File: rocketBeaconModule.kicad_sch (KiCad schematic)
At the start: 38 parts, among them J1 TYPE-C-31-M-12, U1 STM32F401CCU6, U2 CP2102N-Axx-xQFN20, Y1 16MHz

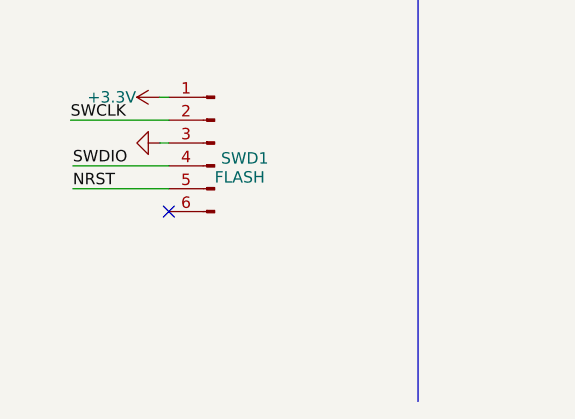
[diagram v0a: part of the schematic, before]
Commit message: added power pads
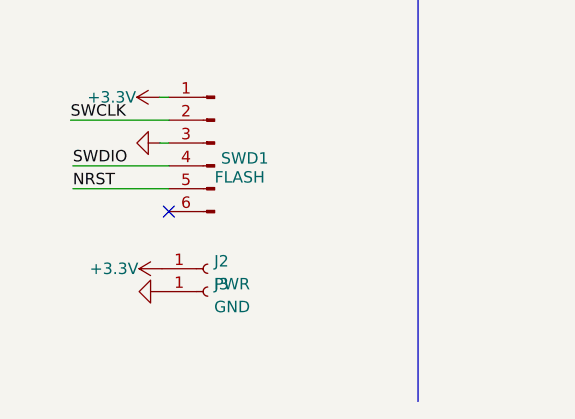
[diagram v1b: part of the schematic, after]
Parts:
- added J2: PWR, TestPoint:TestPoint_THTPad_4.0x4.0mm_Drill2.0mm, symbol Connector:Conn_01x01_Female
- added J3: GND, TestPoint:TestPoint_THTPad_4.0x4.0mm_Drill2.0mm, symbol Connector:Conn_01x01_Female
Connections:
- net +3.3V: now also J2.1 (Pin_1)
- net GND: now also J3.1 (Pin_1)
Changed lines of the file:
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@@
+    (pin "1")
+  )
+  (symbol (lib_id "power:+3.3V") (at 27.432 183.388 90) (unit 1)
+    (in_bom yes) (on_board yes)
+    (property "Reference" "#PWR0116" (id 0) (at 31.242 183.388 0)
+      (effects (font (size 1.27 1.27)) hide)
+    )
+    (property "Value" "+3.3V" (id 1) (at 22.098 183.388 90))
+    (property "Footprint" "" (id 2) (at 27.432 183.388 0)
+      (effects (font (size 1.27 1.27)) hide)
+    )
+    (property "Datasheet" "" (id 3) (at 27.432 183.388 0)
+      (effects (font (size 1.27 1.27)) hide)
+    )
     (pin "1")
   )
@@
     )
     (property "Datasheet" "" (id 3) (at 231.648 80.518 0)
+      (effects (font (size 1.27 1.27)) hide)
+    )
+    (pin "1")
+  )
+  (symbol (lib_id "Connector:Conn_01x01_Female") (at 32.512 183.388 0) (unit 1)
+    (in_bom yes) (on_board yes) (fields_autoplaced)
+    (property "Reference" "J2" (id 0) (at 33.2232 182.5533 0)
+      (effects (font (size 1.27 1.27)) (justify left))
+    )
+    (property "Value" "PWR" (id 1) (at 33.2232 185.0902 0)
+      (effects (font (size 1.27 1.27)) (justify left))
+    )
+    (property "Footprint" "TestPoint:TestPoint_THTPad_4.0x4.0mm_Drill2.0mm" (id 2) (at 32.512 183.388 0)
+      (effects (font (size 1.27 1.27)) hide)
+    )
+    (property "Datasheet" "~" (id 3) (at 32.512 183.388 0)
       (effects (font (size 1.27 1.27)) hide)
     )
@@
     (pin "2")
   )
+  (symbol (lib_id "power:GND") (at 27.432 185.928 270) (unit 1)
+    (in_bom yes) (on_board yes) (fields_autoplaced)
+    (property "Reference" "#PWR0117" (id 0) (at 21.082 185.928 0)
+      (effects (font (size 1.27 1.27)) hide)
+    )
+    (property "Value" "GND" (id 1) (at 22.352 185.928 0)
+      (effects (font (size 1.27 1.27)) hide)
+    )
+    (property "Footprint" "" (id 2) (at 27.432 185.928 0)
+      (effects (font (size 1.27 1.27)) hide)
+    )
+    (property "Datasheet" "" (id 3) (at 27.432 185.928 0)
+      (effects (font (size 1.27 1.27)) hide)
+    )
+    (pin "1")
+  )
   (symbol (lib_id "power:+3.3V") (at 237.236 145.542 90) (unit 1)
     (in_bom yes) (on_board yes)
@@
     )
     (property "Datasheet" "" (id 3) (at 237.236 145.542 0)
+      (effects (font (size 1.27 1.27)) hide)
+    )
+    (pin "1")
+  )
+  (symbol (lib_id "Connector:Conn_01x01_Female") (at 32.512 185.928 0) (unit 1)
+    (in_bom yes) (on_board yes) (fields_autoplaced)
+    (property "Reference" "J3" (id 0) (at 33.2232 185.0933 0)
+      (effects (font (size 1.27 1.27)) (justify left))
+    )
+    (property "Value" "GND" (id 1) (at 33.2232 187.6302 0)
+      (effects (font (size 1.27 1.27)) (justify left))
+    )
+    (property "Footprint" "TestPoint:TestPoint_THTPad_4.0x4.0mm_Drill2.0mm" (id 2) (at 32.512 185.928 0)
+      (effects (font (size 1.27 1.27)) hide)
+    )
+    (property "Datasheet" "~" (id 3) (at 32.512 185.928 0)
       (effects (font (size 1.27 1.27)) hide)
     )
@@
       (reference "#PWR0115") (unit 1) (value "+3.3V") (footprint "")
     )
+    (path "/50559c8e-8b0e-41f0-99d6-b5a806ac8722"
+      (reference "#PWR0116") (unit 1) (value "+3.3V") (footprint "")
+    )
+    (path "/79e3543b-cf5c-49ac-8461-e5ea63f0cfbf"
+      (reference "#PWR0117") (unit 1) (value "GND") (footprint "")
+    )
     (path "/0ce93c00-e125-4297-8f4f-84288d9bed20"
       (reference "C1") (unit 1) (value "4.7uF") (footprint "Capacitor_SMD:C_0603_1608Metric")
@@
       (reference "J1") (unit 1) (value "TYPE-C-31-M-12") (footprint "usbc:HRO_TYPE-C-31-M-12")
     )
+    (path "/64d1ad8a-ccb6-4332-9fde-cca7c83035f2"
+      (reference "J2") (unit 1) (value "PWR") (footprint "TestPoint:TestPoint_THTPad_4.0x4.0mm_Drill2.0mm")
+    )
+    (path "/7d013029-79b1-46c3-8038-ebb027ea4167"
+      (reference "J3") (unit 1) (value "GND") (footprint "TestPoint:TestPoint_THTPad_4.0x4.0mm_Drill2.0mm")
+    )
     (path "/dfcafdf4-f213-4518-865d-ab9ee2b88e54/a901ecb2-8365-4aa2-b92a-22f9aa9420f4"

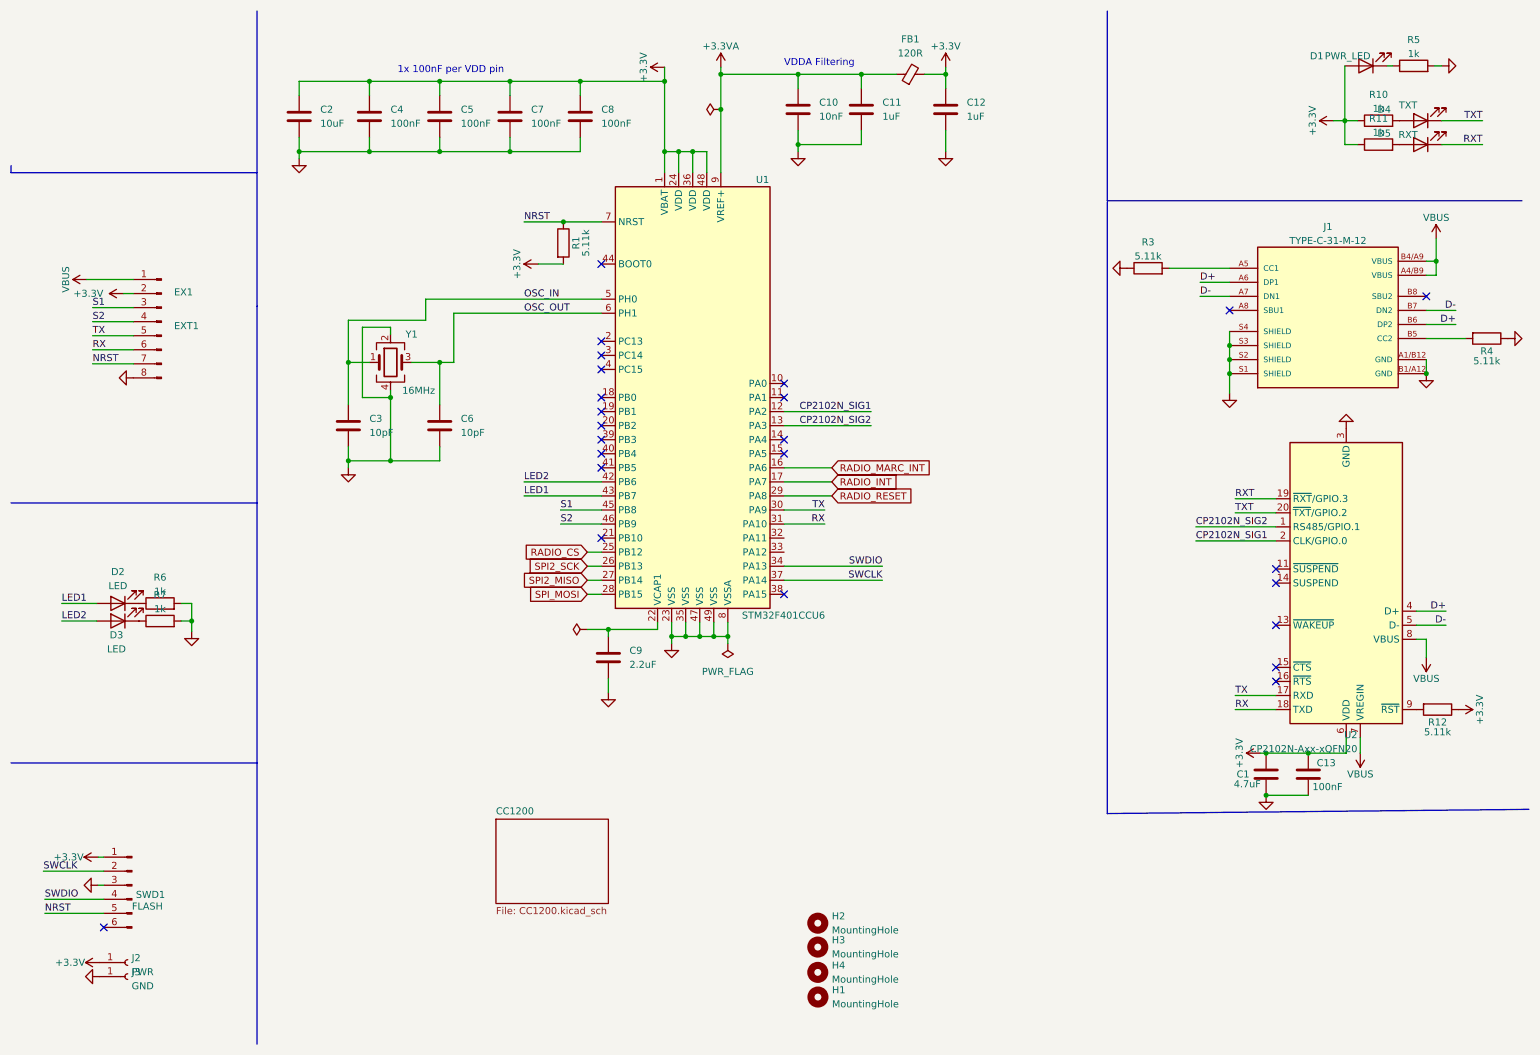
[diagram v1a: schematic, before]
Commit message: V4 Changes Added SKYWORKS +30db 4W FEM Added LM2576 3.9V supply Increased diameter to 60mm Re-routed full board
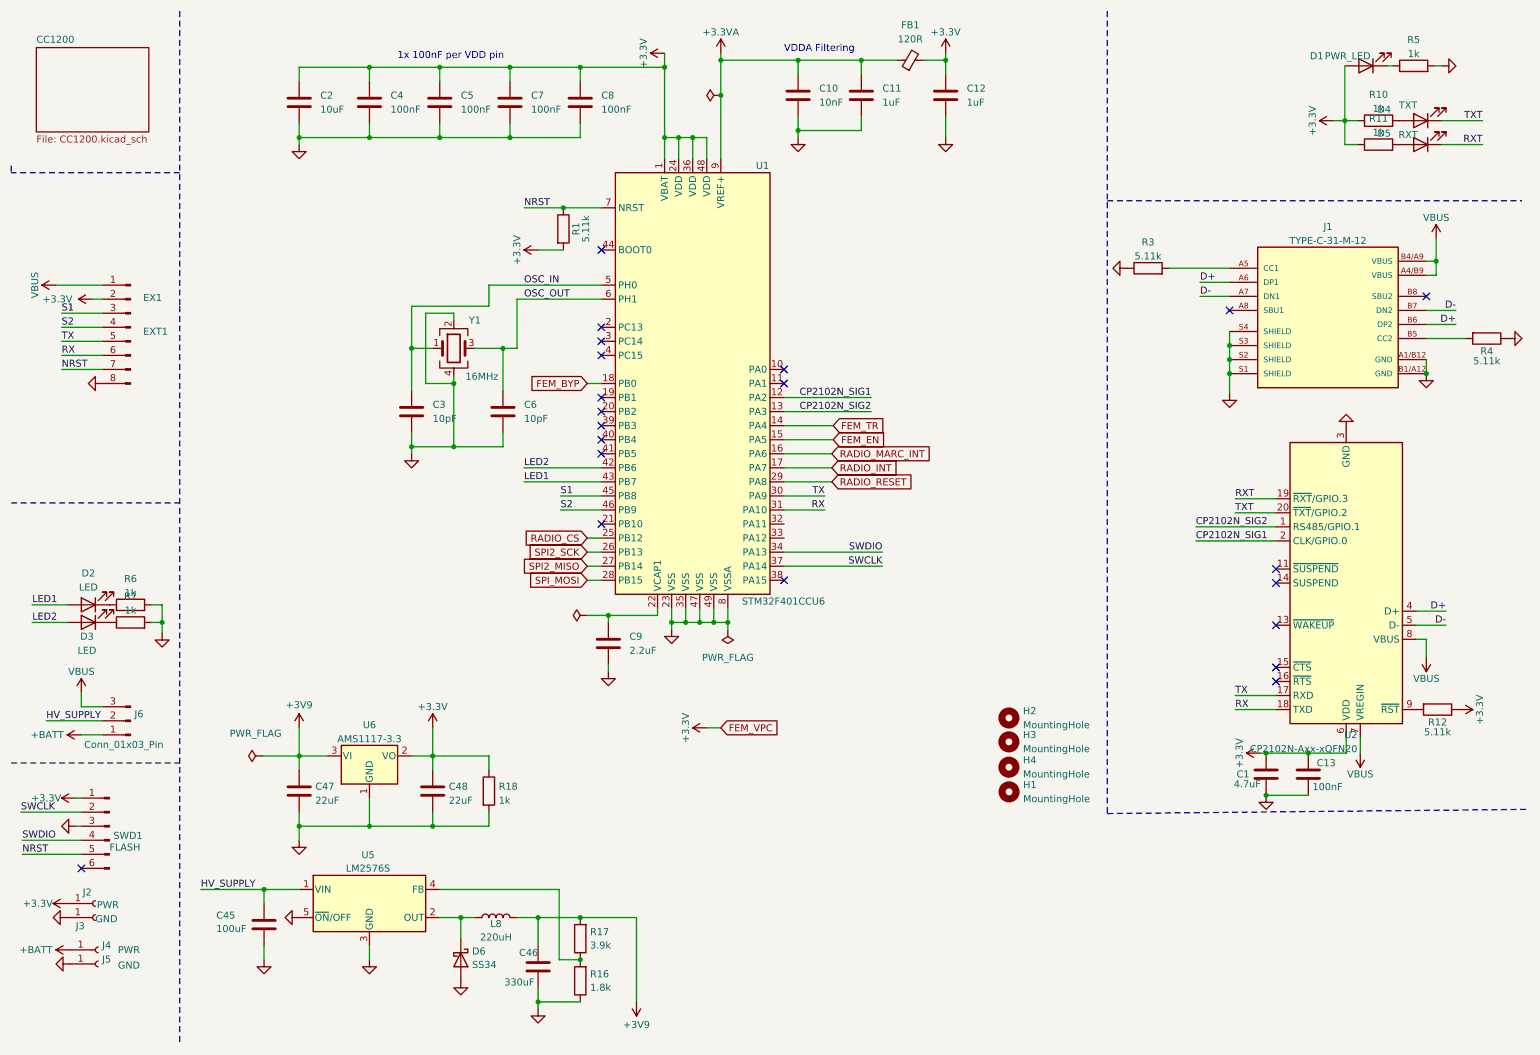
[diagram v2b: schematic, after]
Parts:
- added C45: 100uF, Capacitor_SMD:C_0805_2012Metric, symbol Device:C
- added C46: 330uF, Capacitor_SMD:CP_Elec_10x10.5, symbol Device:C
- added C47, C48: 22uF, Capacitor_SMD:C_0805_2012Metric, symbol Device:C
- added D6: SS34, Diode_SMD:D_SMA, symbol Diode:SS34
- added J4: PWR, TestPoint:TestPoint_THTPad_4.0x4.0mm_Drill2.0mm, symbol Connector:Conn_01x01_Female
- added J5: GND, TestPoint:TestPoint_THTPad_4.0x4.0mm_Drill2.0mm, symbol Connector:Conn_01x01_Female
- added J6: Conn_01x03_Pin, Connector_PinHeader_2.54mm:PinHeader_1x03_P2.54mm_Vertical, symbol Connector:Conn_01x03_Pin
- added L8: 220uH, Capacitor_SMD:C_1206_3216Metric_Pad1.33x1.80mm_HandSolder, symbol Device:L
- added R16: 1.8k, Resistor_SMD:R_0402_1005Metric, symbol Device:R
- added R17: 3.9k, Resistor_SMD:R_0402_1005Metric, symbol Device:R
- added R18: 1k, Resistor_SMD:R_0402_1005Metric, symbol Device:R
- added U5: LM2576S, Package_TO_SOT_SMD:TO-263-5_TabPin3, symbol Regulator_Switching:LM2576S-3.3
- added U6: AMS1117-3.3, Package_TO_SOT_SMD:SOT-223-3_TabPin2, symbol Regulator_Linear:AMS1117-3.3
- C2: LCSC Part C19702 -> c
- SWD1: footprint Connector_PinSocket_1.27mm:PinSocket_1x05_P1.27mm_Vertical -> Connector_PinSocket_2.54mm:PinSocket_1x05_P2.54mm_Vertical
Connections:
- net +3.3V: now also C48.1, R18.1, U6.2 (VO)
- net GND: now also C45.1, C46.1, C47.2, C48.2, D6.2 (A), J5.1 (Pin_1), R16.1, R18.2, U5.3 (GND), U5.5 (~{ON}/OFF), U6.1 (GND)
- net VBUS: now also J6.3 (Pin_3)
- net FEM_TR: now reaches U1.14 (PA4)
- net FEM_EN: now reaches U1.15 (PA5)
- net FEM_BYP: now reaches U1.18 (PB0)
- new net: D6.1 (K), L8.1, U5.2 (OUT)
- new net: R16.2, R17.1, U5.4 (FB)
- new net +3V9: C46.2, C47.1, L8.2, R17.2, U6.3 (VI)
- new net +BATT: J4.1 (Pin_1), J6.1 (Pin_1)
- new net HV_SUPPLY: C45.2, J6.2 (Pin_2), U5.1 (VIN)
- no-connect marks 24 -> 21
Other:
- moved on the sheet: C10, C11, C12, C2, C3, C4, C5, C6, C7, C8, C9, D2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

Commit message: Adjusted some component footprints and part numbers Increased size of inductor and repositioned generated gbrs, drills, bom and cpl (up to date)
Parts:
- EX1: LCSC Part C124378 -> C132510
- L8: footprint Capacitor_SMD:C_1206_3216Metric_Pad1.33x1.80mm_HandSolder -> Inductor_SMD:L_Sunlord_SWRB1207S
- SWD1: LCSC Part C124378 -> (none)
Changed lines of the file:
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@@
 			)
 		)
-		(property "Footprint" "Capacitor_SMD:C_1206_3216Metric_Pad1.33x1.80mm_HandSolder"
+		(property "Footprint" "Inductor_SMD:L_Sunlord_SWRB1207S"
 			(at 99.06 175.26 0)
 			(effects
@@
 			)
 		)
-		(property "LCSC Part" "C124378"
+		(property "LCSC Part" ""
 			(at 29.21 158.75 0)
 			(effects
@@
 			)
 		)
-		(property "LCSC Part" "C124378"
+		(property "LCSC Part" "C132510"
 			(at 33.02 68.58 0)
 			(effects

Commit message: switched pins on ribbon cable to connect evenly with FC when flipped
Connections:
- net +3.3V: now also EX1.7 (Pin_7); no longer EX1.2 (Pin_2)
- net GND: now also EX1.1 (Pin_1); no longer EX1.8 (Pin_8)
- net NRST: now also EX1.2 (Pin_2); no longer EX1.7 (Pin_7)
- net RX: now also EX1.3 (Pin_3); no longer EX1.6 (Pin_6)
- net S1: now also EX1.6 (Pin_6); no longer EX1.3 (Pin_3)
- net S2: now also EX1.5 (Pin_5); no longer EX1.4 (Pin_4)
- net TX: now also EX1.4 (Pin_4); no longer EX1.5 (Pin_5)
- net VBUS: now also EX1.8 (Pin_8); no longer EX1.1 (Pin_1)
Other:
- moved on the sheet: EX1

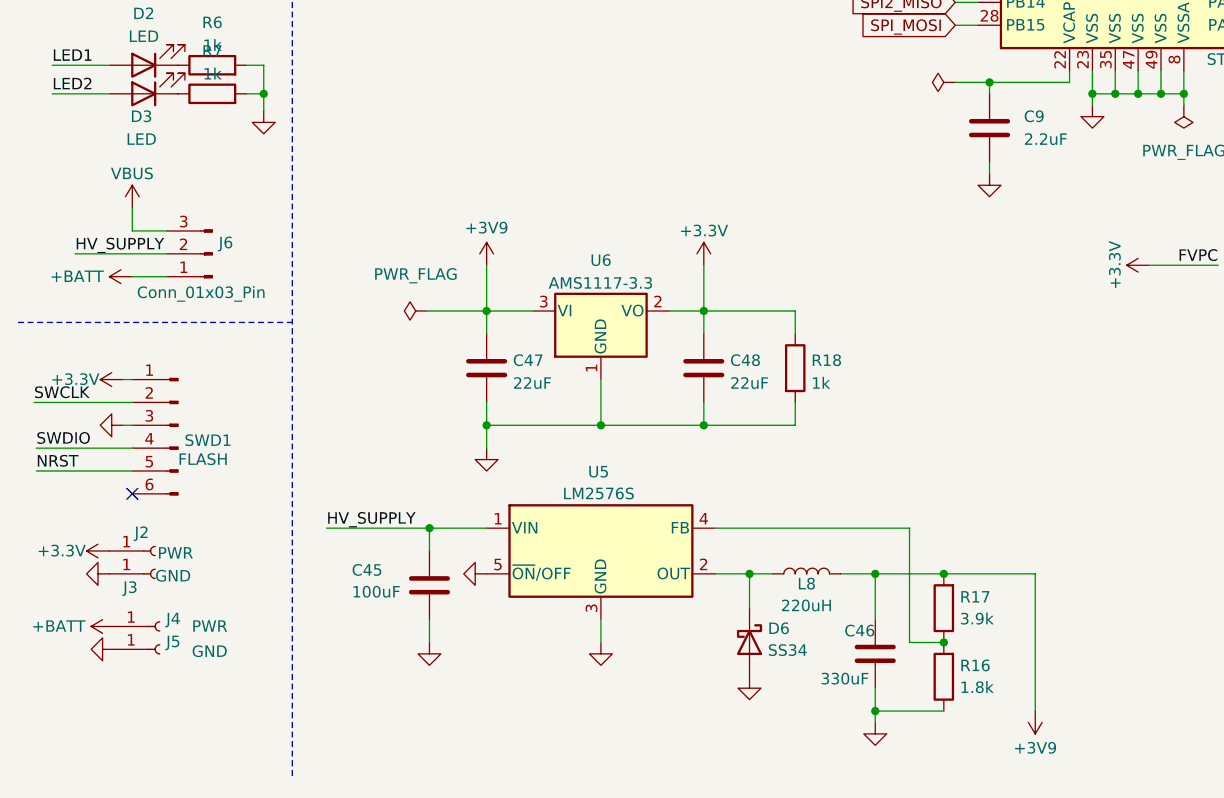
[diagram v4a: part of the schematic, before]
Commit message: removed old PA
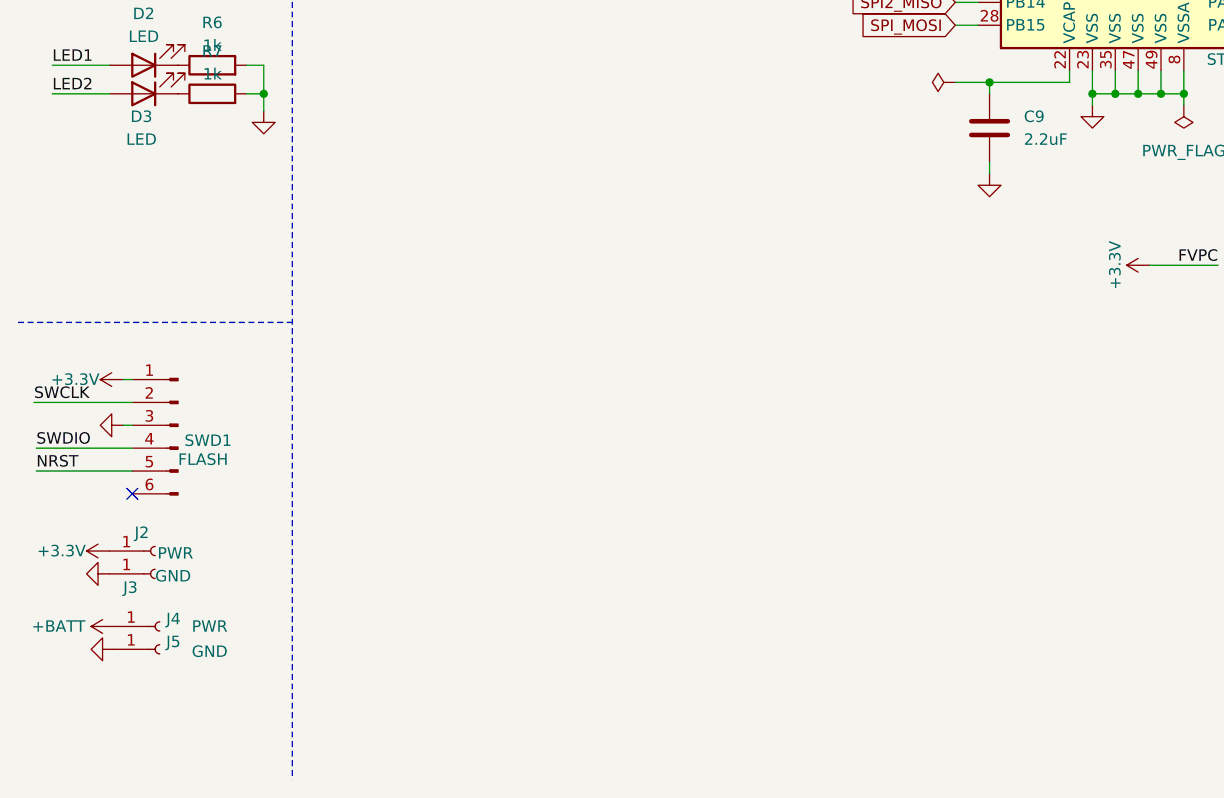
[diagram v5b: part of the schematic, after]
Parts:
- removed C45: 100uF, Capacitor_SMD:C_0805_2012Metric, symbol Device:C
- removed C46: 330uF, Capacitor_SMD:CP_Elec_10x10.5, symbol Device:C
- removed C47, C48: 22uF, Capacitor_SMD:C_0805_2012Metric, symbol Device:C
- removed D6: SS34, Diode_SMD:D_SMA, symbol Diode:SS34
- removed J6: Conn_01x03_Pin, Connector_PinHeader_2.54mm:PinHeader_1x03_P2.54mm_Vertical, symbol Connector:Conn_01x03_Pin
- removed L8: 220uH, Inductor_SMD:L_Sunlord_SWRB1207S, symbol Device:L
- removed R16: 1.8k, Resistor_SMD:R_0402_1005Metric, symbol Device:R
- removed R17: 3.9k, Resistor_SMD:R_0402_1005Metric, symbol Device:R
- removed R18: 1k, Resistor_SMD:R_0402_1005Metric, symbol Device:R
- removed U5: LM2576S, Package_TO_SOT_SMD:TO-263-5_TabPin3, symbol Regulator_Switching:LM2576S-3.3
- removed U6: AMS1117-3.3, Package_TO_SOT_SMD:SOT-223-3_TabPin2, symbol Regulator_Linear:AMS1117-3.3
